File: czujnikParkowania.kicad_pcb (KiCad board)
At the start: 2 copper layers, 46 parts, among them J1 Screw_Terminal_01x03, Q1 BC817, Q2 IRF7404, Q3 BC817, Q4 BC817, Q5 BC817, SW1 SW_Push, U1 DC56-11SEKWA, U2 LM7805_TO220, U3 HC-SR04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

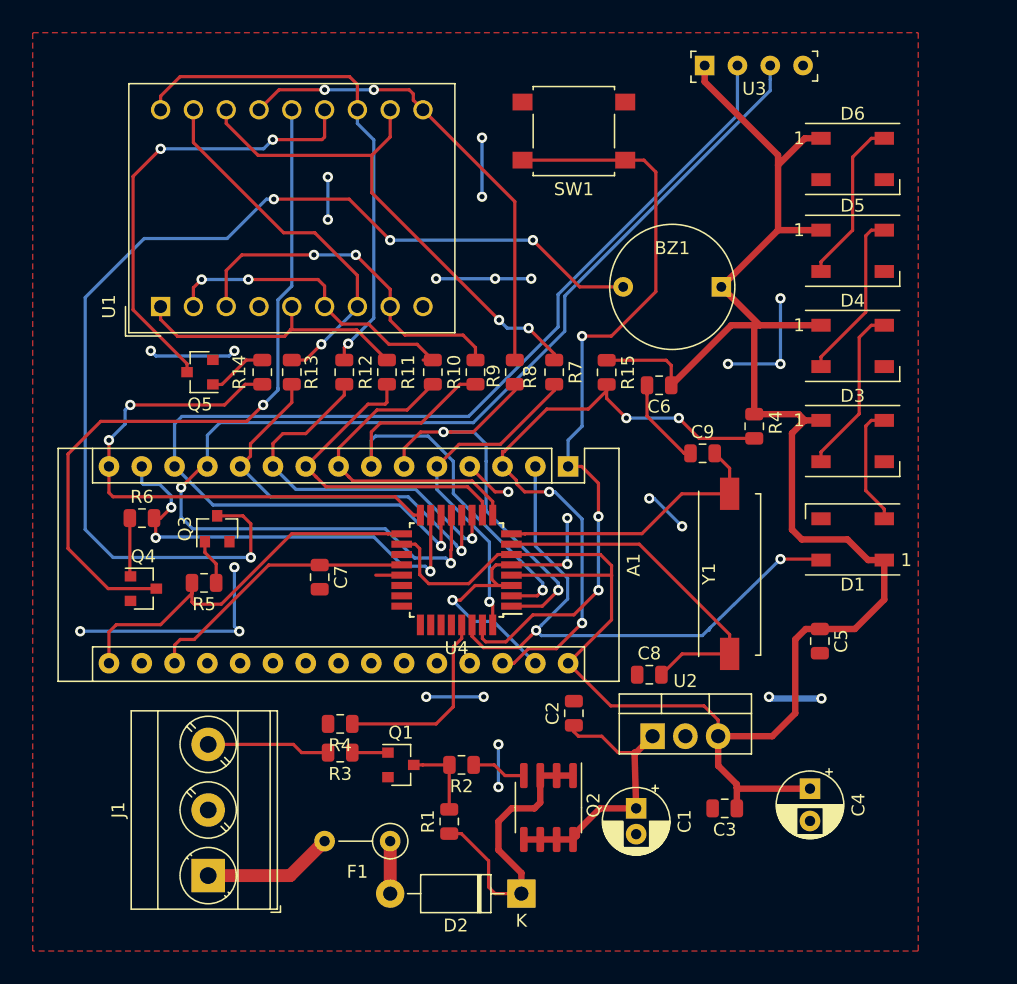
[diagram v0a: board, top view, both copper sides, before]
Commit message: added capacitors
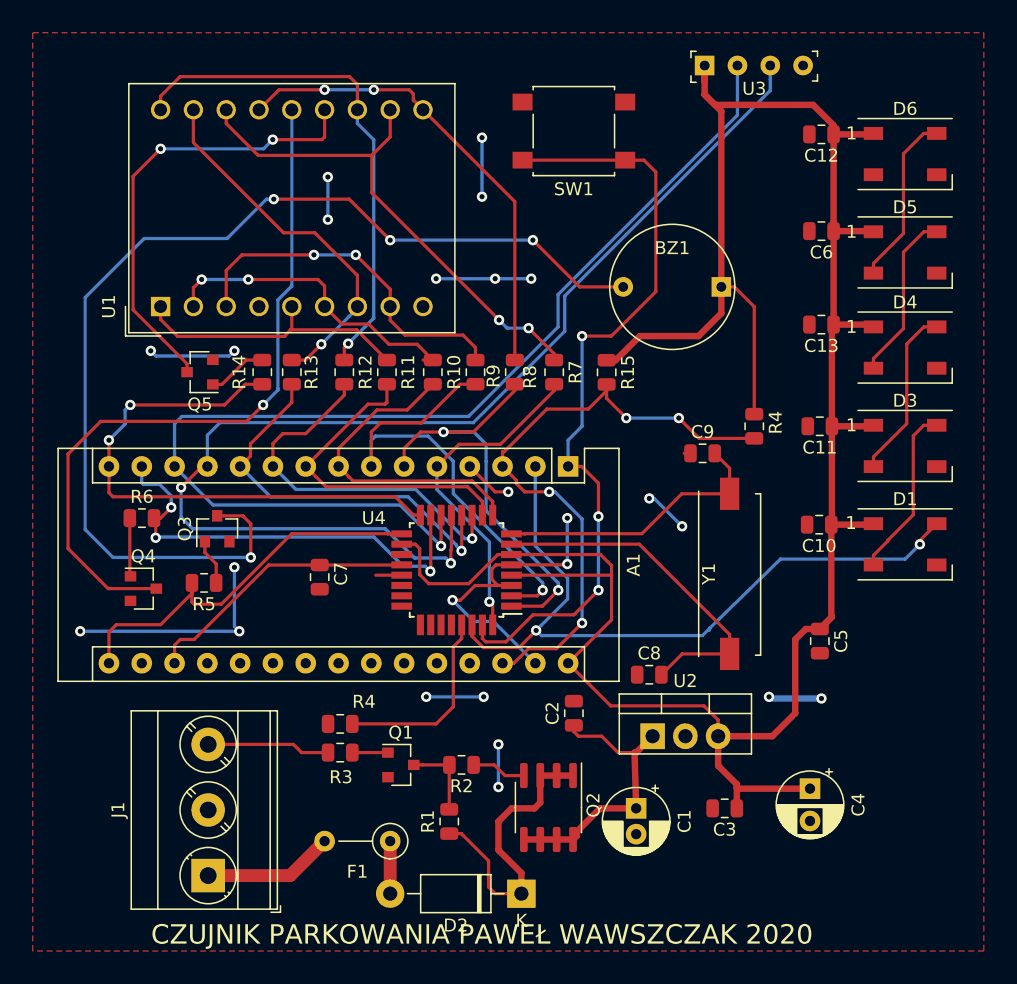
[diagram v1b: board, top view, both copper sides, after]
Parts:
- added C10: 100n, Capacitor_SMD:C_0805_2012Metric, F.Cu at (76.2, 55.9)
- added C11: 100n, Capacitor_SMD:C_0805_2012Metric, F.Cu at (76.2, 48.3)
- added C12: 100n, Capacitor_SMD:C_0805_2012Metric, F.Cu at (76.3, 25.7)
- added C13: 100n, Capacitor_SMD:C_0805_2012Metric, F.Cu at (76.3, 40.4)
- moved C6 17.3 mm to (76.3, 33.1)
- moved D1 4.08 mm to (82.8, 57.4), turned to 0 degrees
- moved D3 4.08 mm to (82.8, 49.8)
- moved D6 4.08 mm to (82.8, 27.2)
- moved D4 4.07 mm to (82.8, 42.2)
- moved D5 4.07 mm to (82.8, 34.8)
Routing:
- net +5V: track 169.5 -> 188.5 mm
- net GND: track 101.2 -> 85.6 mm, vias 27 -> 24
- net /RGB_DI: track 46.5 -> 56.7 mm
- net Net-(D1-Pad2): track 9.39 -> 13.4 mm
- net Net-(D5-Pad2): track 12.9 -> 13.4 mm
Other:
- board text added: "CZUJNIK PARKOWANIA PAWEŁ WAWSZCZAK 2020"

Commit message: added GND plane on back
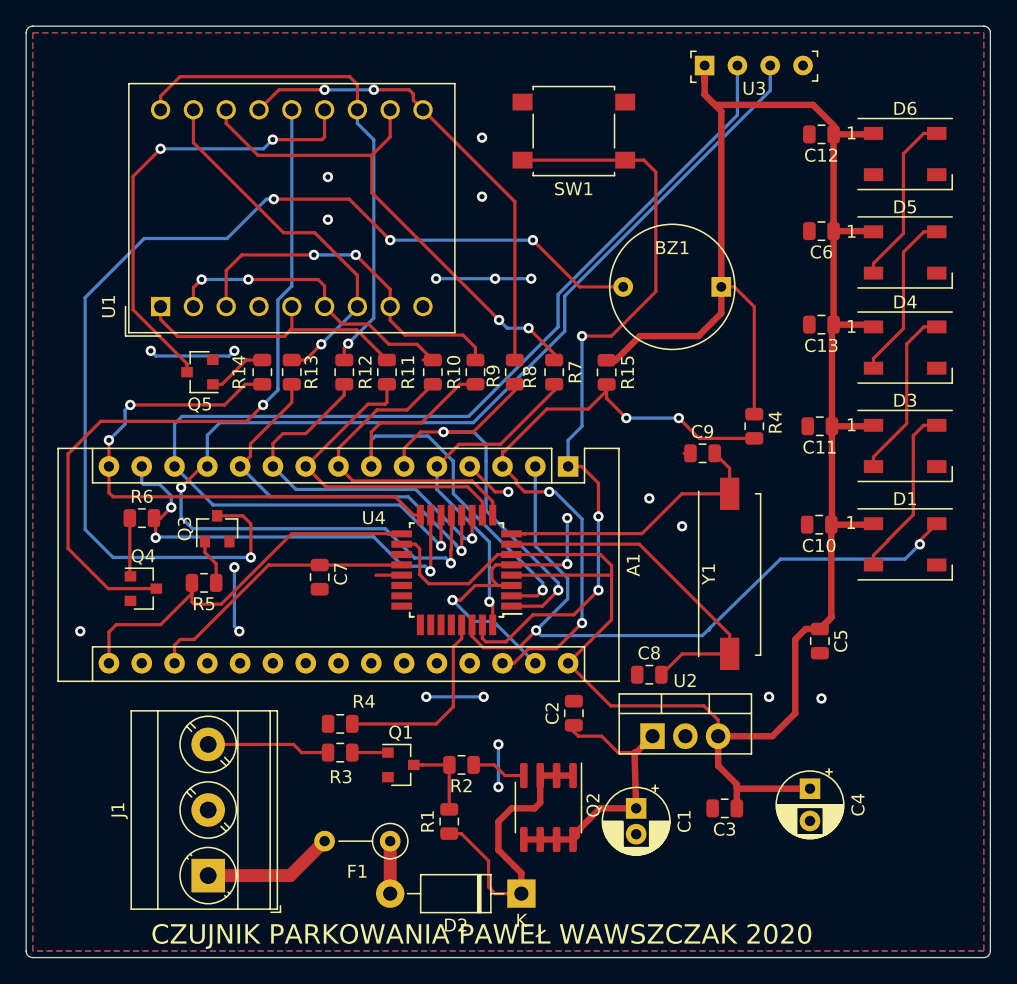
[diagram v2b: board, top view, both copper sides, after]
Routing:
- net GND: track 85.6 -> 58.0 mm
- added copper zone on B.Cu, net GND
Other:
- board outline added: 74.7 x 72.1 mm
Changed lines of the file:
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@@
   (general
     (thickness 1.6)
-    (drawings 1)
-    (tracks 587)
+    (drawings 9)
+    (tracks 581)
     (zones 0)
     (modules 50)
@@
   )
   (setup
-    (last_trace_width 0.5)
+    (last_trace_width 0.25)
     (user_trace_width 0.5)
     (user_trace_width 1)
@@
     )
   )
+  (gr_line (start 15.24 89.408) (end 88.9 89.408) (layer Edge.Cuts) (width 0.05))
+  (gr_line (start 14.732 17.78) (end 14.732 88.9) (layer Edge.Cuts) (width 0.05))
+  (gr_line (start 88.9 17.272) (end 15.24 17.272) (layer Edge.Cuts) (width 0.05))
+  (gr_line (start 89.408 88.9) (end 89.408 17.78) (layer Edge.Cuts) (width 0.05))
+  (gr_arc (start 88.9 88.9) (end 88.9 89.408) (angle -90) (layer Edge.Cuts) (width 0.05))
+  (gr_arc (start 15.24 88.9) (end 14.732 88.9) (angle -90) (layer Edge.Cuts) (width 0.05))
+  (gr_arc (start 15.24 17.78) (end 15.24 17.272) (angle -90) (layer Edge.Cuts) (width 0.05))
+  (gr_arc (start 88.9 17.78) (end 89.408 17.78) (angle -90) (layer Edge.Cuts) (width 0.05))
   (gr_text "CZUJNIK PARKOWANIA PAWEŁ WAWSZCZAK 2020" (at 50.038 87.63) (layer F.SilkS)
     (effects (font (size 1.5 1.5) (thickness 0.3)))
@@
   (via (at 72.263 69.215) (size 0.8) (drill 0.4) (layers F.Cu B.Cu) (net 4))
   (segment (start 72.39 69.342) (end 72.263 69.215) (width 0.5) (layer B.Cu) (net 4))
-  (segment (start 76.327 69.342) (end 72.39 69.342) (width 0.5) (layer B.Cu) (net 4))
   (segment (start 54.1655 66.6115) (end 50.927 63.373) (width 0.25) (layer B.Cu) (net 4))
   (via (at 47.752 61.722) (size 0.8) (drill 0.4) (layers F.Cu B.Cu) (net 4))
@@
   (segment (start 30.861 63.754) (end 31.242 64.135) (width 0.25) (layer B.Cu) (net 4))
   (segment (start 30.861 59.182) (end 30.861 63.754) (width 0.25) (layer B.Cu) (net 4))
-  (segment (start 18.923 64.135) (end 31.242 64.135) (width 0.25) (layer B.Cu) (net 4))
   (via (at 30.861 42.418) (size 0.8) (drill 0.4) (layers F.Cu B.Cu) (net 4))
   (via (at 24.384 42.418) (size 0.8) (drill 0.4) (layers F.Cu B.Cu) (net 4))
@@
   (via (at 65.532 56.007) (size 0.8) (drill 0.4) (layers F.Cu B.Cu) (net 4))
   (via (at 62.992 53.848) (size 0.8) (drill 0.4) (layers F.Cu B.Cu) (net 4))
-  (segment (start 63.373 53.848) (end 62.992 53.848) (width 0.25) (layer B.Cu) (net 4))
-  (segment (start 65.532 56.007) (end 63.373 53.848) (width 0.25) (layer B.Cu) (net 4))
   (segment (start 43.815 59.7915) (end 41.8085 59.7915) (width 0.25) (layer F.Cu) (net 4))
   (via (at 45.72 69.215) (size 0.8) (drill 0.4) (layers F.Cu B.Cu) (net 4))
@@
   (segment (start 45.72 69.215) (end 50.165 69.215) (width 0.25) (layer B.Cu) (net 4))
   (via (at 50.038 25.908) (size 0.8) (drill 0.4) (layers F.Cu B.Cu) (net 4))
-  (segment (start 50.038 25.908) (end 50.038 30.48) (width 0.25) (layer B.Cu) (net 4))
   (via (at 51.054 36.83) (size 0.8) (drill 0.4) (layers F.Cu B.Cu) (net 4))
   (segment (start 51.054 36.83) (end 53.848 36.83) (width 0.25) (layer B.Cu) (net 4))
   (segment (start 51.054 36.83) (end 46.482 36.83) (width 0.25) (layer B.Cu) (net 4))
   (via (at 38.1 32.258) (size 0.8) (drill 0.4) (layers F.Cu B.Cu) (net 4))
-  (segment (start 38.1 28.956) (end 38.1 32.258) (width 0.25) (layer B.Cu) (net 4))
   (via (at 51.308 72.898) (size 0.8) (drill 0.4) (layers F.Cu B.Cu) (net 4))
   (segment (start 51.308 72.898) (end 51.308 76.2) (width 0.25) (layer B.Cu) (net 4))
@@
   (segment (start 26.2255 65.2145) (end 26.2255 66.6115) (width 0.25) (layer F.Cu) (net 67))
   (segment (start 26.67 64.77) (end 26.2255 65.2145) (width 0.25) (layer F.Cu) (net 67))
-  (zone (net 0) (net_name "") (layer Edge.Cuts) (hatch edge 0.508)
+  (zone (net 4) (net_name GND) (layer F.Cu) (hatch edge 0.508)
     (connect_pads (clearance 0.508))
     (min_thickness 0.254)
@@
     )
   )
-  (zone (net 4) (net_name GND) (layer F.Cu) (hatch edge 0.508)
+  (zone (net 4) (net_name GND) (layer B.Cu) (hatch edge 0.508)
     (connect_pads (clearance 0.508))
     (min_thickness 0.254)

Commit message: schematic reset pin bug fix
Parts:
- R4: value 1k -> 10k
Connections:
- R4 pad 1: Net-(R4-Pad1) -> +5V
- R4 pad 2: GND -> Net-(R4-Pad2)
- U4 pad 29: Net-(R4-Pad1) -> Net-(R4-Pad2)
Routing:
- net Net-(R4-Pad2): track 0.00 -> 19.2 mm
- net +5V: track 188.5 -> 207.6 mm
- net Net-(R4-Pad1): track 15.0 -> 0.00 mm
- net GND: track 58.0 -> 62.8 mm, vias 24 -> 40
